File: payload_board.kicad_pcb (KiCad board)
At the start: 4 copper layers, 100 x 100 mm, 94 parts, among them IC1 RP2040_QFN56, IC2 AZ1117CH-3.3TRG1, J1 Cam_PicoLock, J12 5025700893, J12 FC Breakout, J15 SWC, J2 Cam_Conn, J2 Conn_ARM_JTAG_SWD_10, J3 Antenna_Conn, J4 usb jumper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

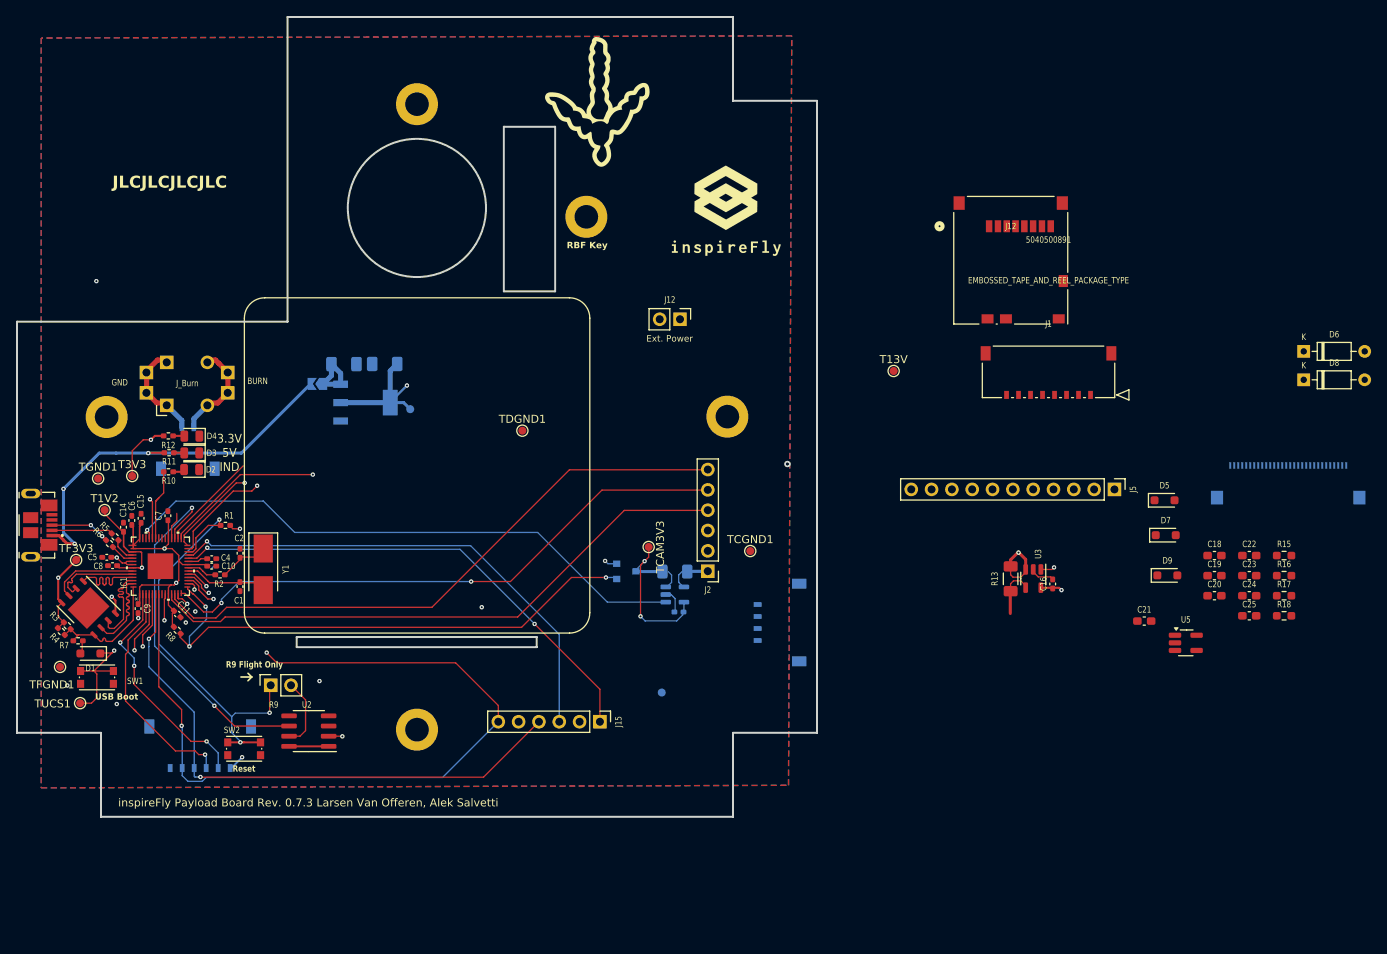
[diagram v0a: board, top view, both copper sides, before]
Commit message: Updated component placements and footprints
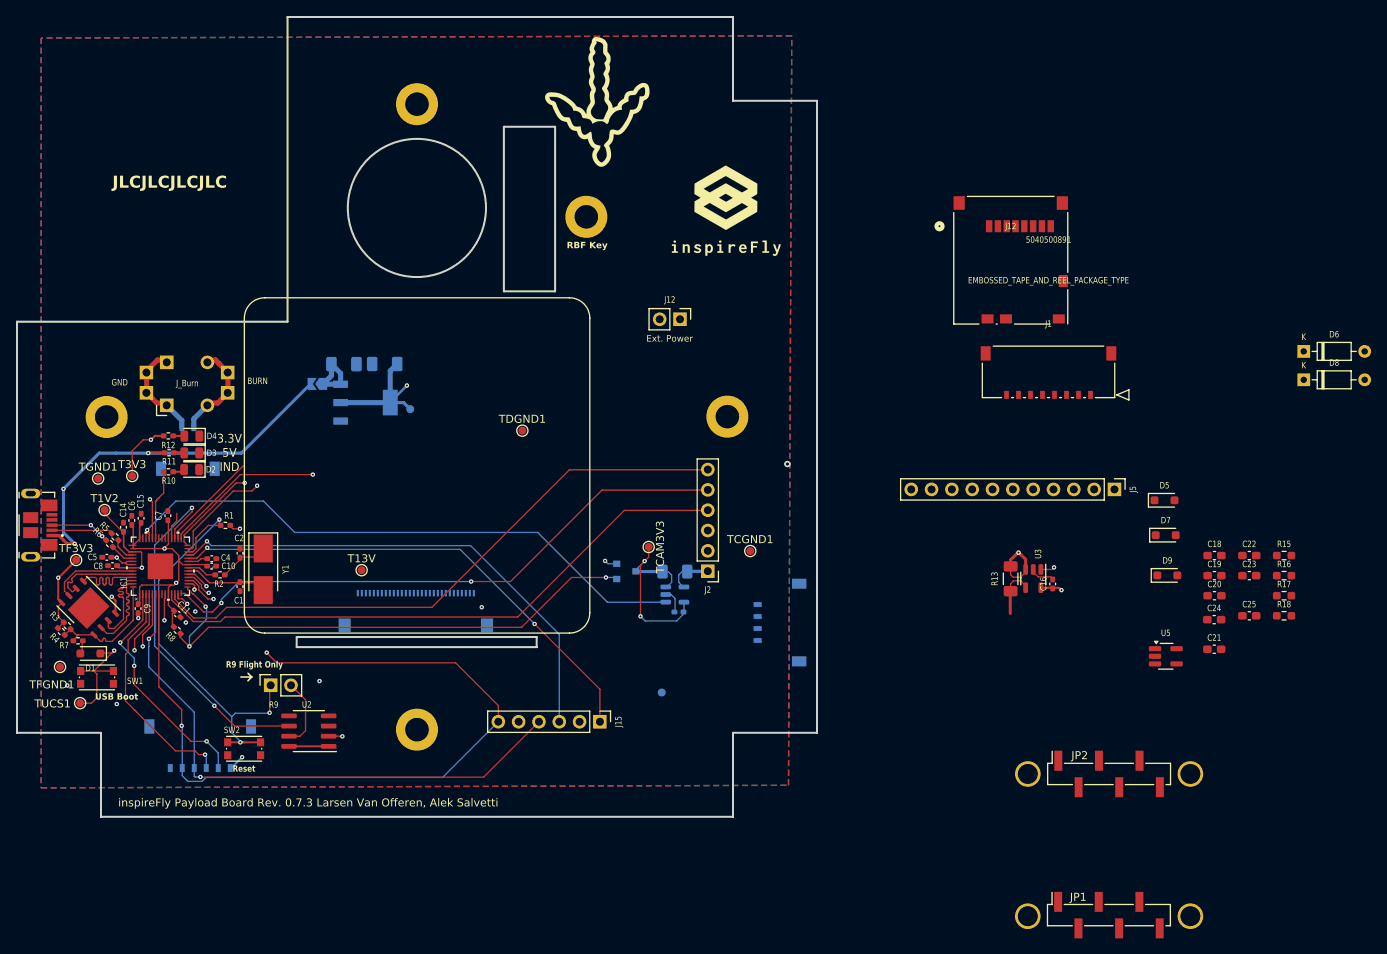
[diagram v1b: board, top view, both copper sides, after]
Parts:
- added ?: , , F.Cu at (159.7, 107.6)
- added ?: , , F.Cu at (139.3, 107.6)
- added ?: , , F.Cu at (159.7, 125.4)
- added ?: , , F.Cu at (139.3, 125.4)
- added JP1: , Connector_PinHeader_2.54mm:PinHeader_1x06_P2.54mm_Vertical_SMD_Pin1Right, F.Cu at (149.5, 125.3)
- added JP2: , Connector_PinHeader_2.54mm:PinHeader_1x06_P2.54mm_Vertical_SMD_Pin1Right, F.Cu at (149.5, 107.6)
- moved U6 110.2 mm to (62.8, 87.5)
- moved T13V 71.0 mm to (56.1, 82.2)
- moved C21 9.43 mm to (162.7, 92.0)
- moved C24 5.31 mm to (162.6, 88.3)
- moved U5 3.01 mm to (156.6, 92.9)
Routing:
- net GND: vias 9 -> 8
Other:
- board text added: "Keep Together. Mounting for IMU"

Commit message: Updated display footprints to reflect avaliability
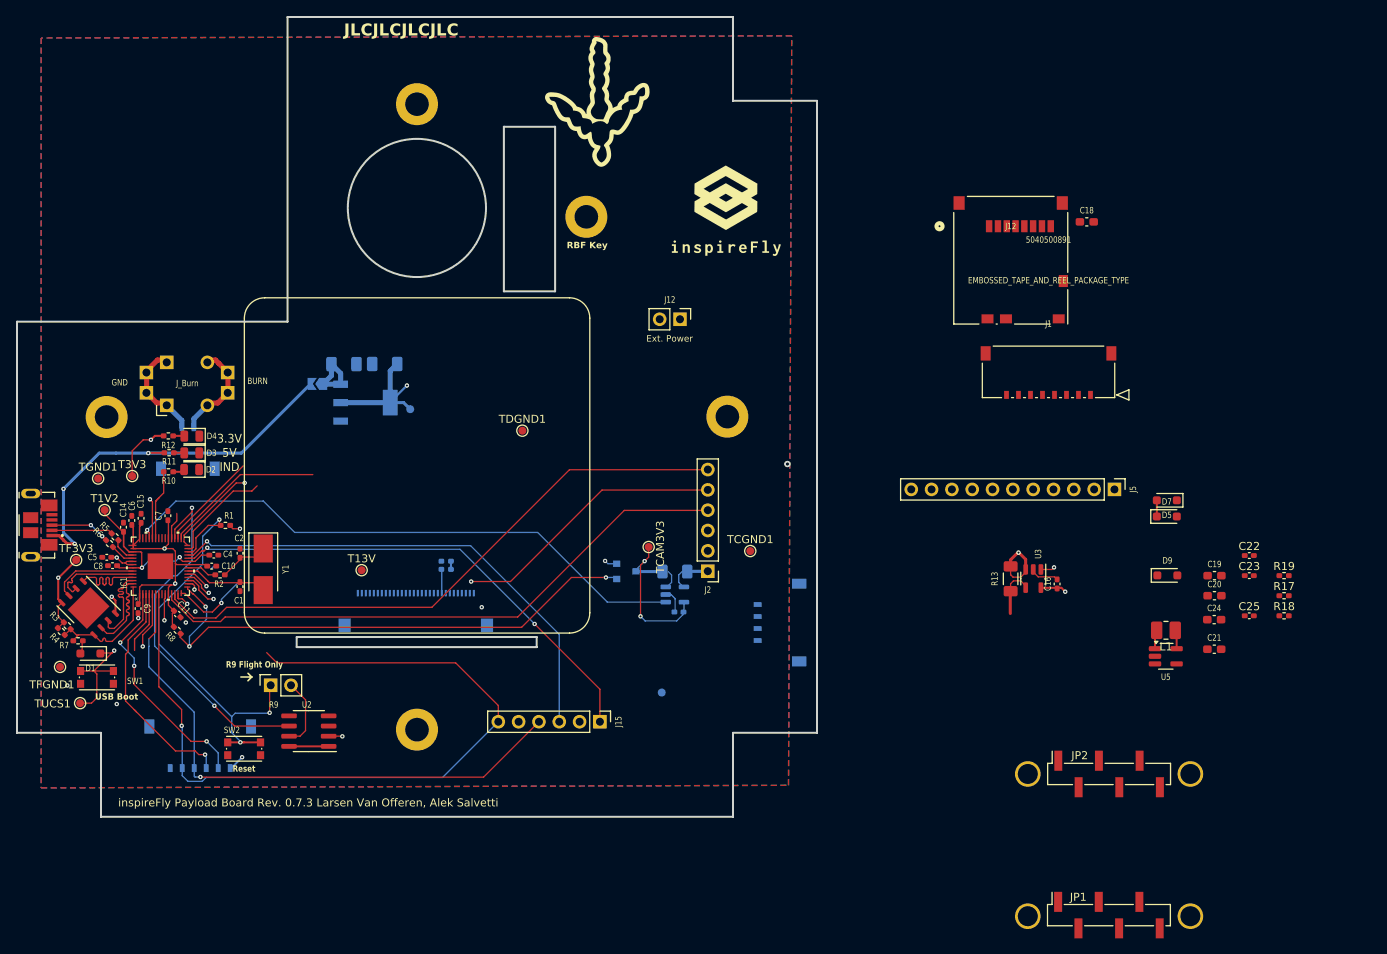
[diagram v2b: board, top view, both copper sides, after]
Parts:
- removed D6, D8: 1N4148, Diode_THT:D_DO-35_SOD27_P7.62mm_Horizontal
- added L1: 10uH/1A, Inductor_SMD:L_1008_2520Metric_Pad1.43x2.20mm_HandSolder, F.Cu at (156.6, 89.7)
- added R16: 300k, Resistor_SMD:R_0402_1005Metric_Pad0.72x0.64mm_HandSolder, B.Cu at (66.6, 81.0)
- C19: value 10u -> 10uF
- C22, C23, C25: footprint Capacitor_SMD:C_0603_1608Metric_Pad1.08x0.95mm_HandSolder -> Capacitor_SMD:C_0402_1005Metric_Pad0.74x0.62mm_HandSolder
- J2: value Conn_ARM_JTAG_SWD_10 -> (none)
- J5: value usb jumper -> (none)
- R15: value 600k -> 300k; footprint Resistor_SMD:R_0603_1608Metric_Pad0.98x0.95mm_HandSolder -> Resistor_SMD:R_0402_1005Metric_Pad0.72x0.64mm_HandSolder; moved to B.Cu
- R17, R18: footprint Resistor_SMD:R_0603_1608Metric_Pad0.98x0.95mm_HandSolder -> Resistor_SMD:R_0402_1005Metric_Pad0.72x0.64mm_HandSolder
- R19: renamed from R16; footprint Resistor_SMD:R_0603_1608Metric_Pad0.98x0.95mm_HandSolder -> Resistor_SMD:R_0402_1005Metric_Pad0.72x0.64mm_HandSolder
- moved R15 104.8 mm to (66.6, 82.0), turned to 180 degrees
- moved C18 44.7 mm to (146.7, 38.6)
- moved D7 2.34 mm to (156.7, 75.4)
- moved C16 0.55 mm to (143.0, 83.9)
- moved C4 0.52 mm to (37.6, 80.3)
- moved D5 0.29 mm to (156.7, 73.4), turned to 180 degrees
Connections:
- C19 pad 1: +3.3V -> DIN-
- C23 pad 2: +3.3V -> DIN-
- C24 pad 2: +3.3V -> DIN-
- R15 pad 1: GND -> Net-(R15-Pad1)
- U5 pad 4: +3.3V -> DIN-
- U5 pad 5: +3.3V -> DIN-
- U6 pad P$27: +3.3V -> DIN-
- U6 pad P$4: +3.3V -> DIN-
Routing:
- net SPI1_SCK_Cam: track 74.6 -> 2.08 mm
- net Disp_RST: track 62.9 -> 3.42 mm
- net I2C1_SDA: track 66.6 -> 7.88 mm, vias 2 -> 0
- net I2C1_SCL: track 63.2 -> 7.13 mm
- net UART1_TX: track 124.6 -> 71.6 mm, vias 2 -> 1
- net Disp_DC: track 54.3 -> 4.89 mm
- net ADC0: track 53.0 -> 6.86 mm
- net SD_IND: track 47.4 -> 3.74 mm
- net SPI0_SCK: track 52.6 -> 20.2 mm, vias 1 -> 0
- net SPI0_MISO: track 42.3 -> 13.1 mm, vias 1 -> 0
- net SPI1_MOSI_Cam: track 73.3 -> 44.3 mm
- net /USBBOOT: track 31.7 -> 17.0 mm
- net UART1_RX: track 114.7 -> 100.6 mm, vias 2 -> 1
- net Net-(U6-IREF): track 0.00 -> 3.00 mm
- net Net-(D9-A): track 0.00 -> 2.38 mm
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
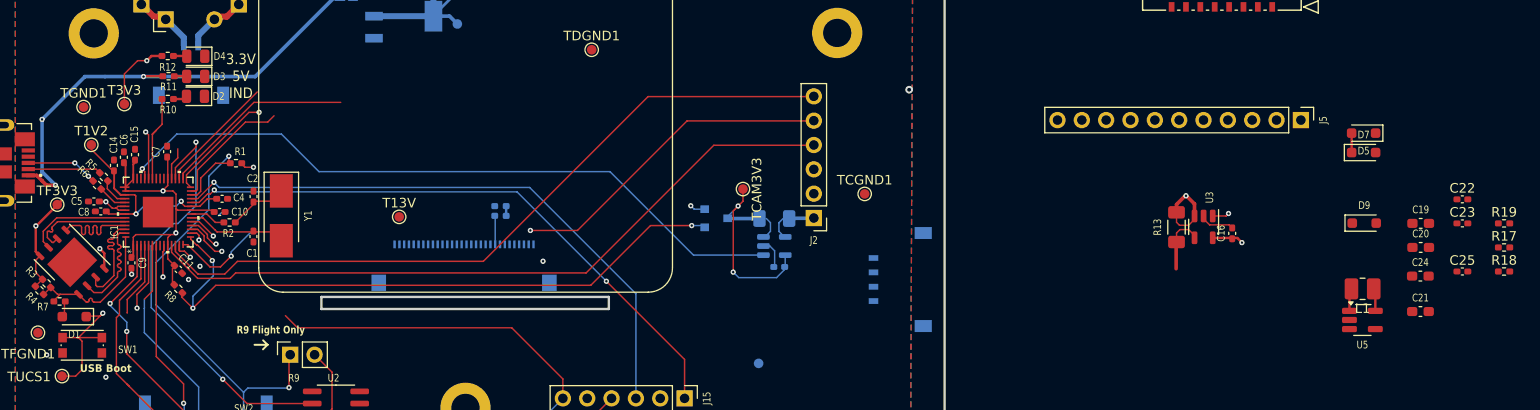
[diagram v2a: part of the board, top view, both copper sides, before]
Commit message: Changed the orientation of the connector to align, and moved a couple of the components Will continue tomorrow
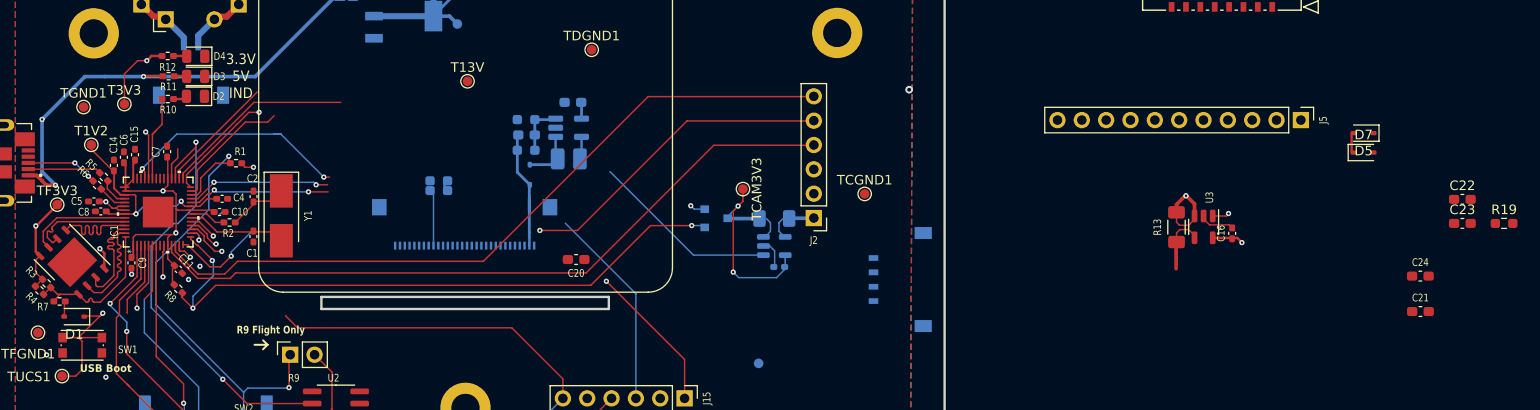
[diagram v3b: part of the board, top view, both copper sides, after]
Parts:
- C19, L1, U5: moved to B.Cu
- C22, C23: footprint Capacitor_SMD:C_0402_1005Metric_Pad0.74x0.62mm_HandSolder -> Capacitor_SMD:C_0603_1608Metric_Pad1.08x0.95mm_HandSolder
- C25: footprint Capacitor_SMD:C_0402_1005Metric_Pad0.74x0.62mm_HandSolder -> Capacitor_SMD:C_0603_1608Metric_Pad1.08x0.95mm_HandSolder; moved to B.Cu
- D1, D5, D7: footprint Diode_SMD:D_SOD-323_HandSoldering -> Diode_SMD:D_SOD-323
- D9: footprint Diode_SMD:D_SOD-323_HandSoldering -> Diode_SMD:D_SOD-323; moved to B.Cu
- R15, R16, R19: footprint Resistor_SMD:R_0402_1005Metric_Pad0.72x0.64mm_HandSolder -> Resistor_SMD:R_0603_1608Metric_Pad0.98x0.95mm_HandSolder
- R17, R18: footprint Resistor_SMD:R_0402_1005Metric_Pad0.72x0.64mm_HandSolder -> Resistor_SMD:R_0603_1608Metric_Pad0.98x0.95mm_HandSolder; moved to B.Cu
- moved R18 103.3 mm to (69.3, 72.0), turned to 180 degrees
- moved R17 102.6 mm to (69.3, 75.2)
- moved C25 98.7 mm to (69.4, 73.6)
- moved C19 89.4 mm to (74.2, 70.2), turned to 180 degrees
- moved C20 88.1 mm to (74.5, 86.6), turned to 180 degrees
- moved D9 87.2 mm to (69.7, 77.8), turned to 90 degrees
- moved U5 85.2 mm to (73.8, 72.8)
- moved L1 83.9 mm to (73.8, 76.1)
- moved T13V 15.8 mm to (63.2, 68.0)
- moved R15 6.96 mm to (60.2, 79.4)
- moved R16 6.96 mm to (60.2, 78.4)
- moved U6 4.77 mm to (62.9, 82.7), turned to 180 degrees
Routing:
- net SWCLK: track 63.4 -> 30.5 mm, vias 2 -> 3
- net ADC1: track 72.8 -> 44.5 mm, vias 1 -> 2
- net SWDIO: track 62.9 -> 36.4 mm, vias 1 -> 2
- net +13V: track 0.00 -> 13.3 mm
- net Net-(U5-FB): track 0.00 -> 5.42 mm
- net Net-(D9-A): track 2.38 -> 5.54 mm
- net Net-(U6-IREF): track 3.00 -> 5.77 mm
- net DIN-: track 8.48 -> 10.2 mm
- net SPI1_MOSI_Cam: track 44.3 -> 43.4 mm
- net Cam_RST: vias 4 -> 3

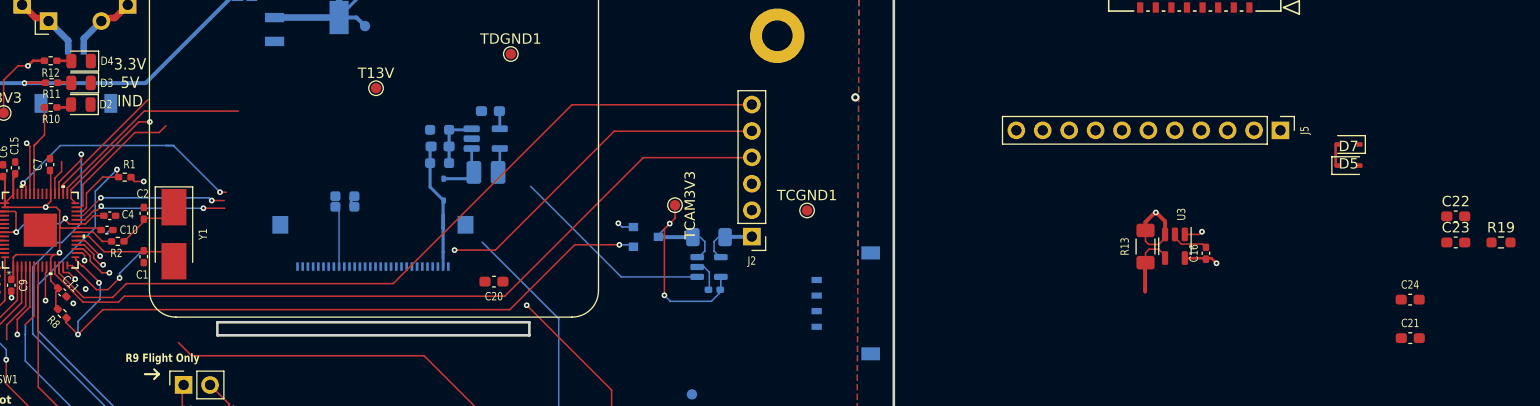
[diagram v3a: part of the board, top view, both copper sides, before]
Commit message: Rotated it back (by bad i dont know how to read schematics) and added some connections
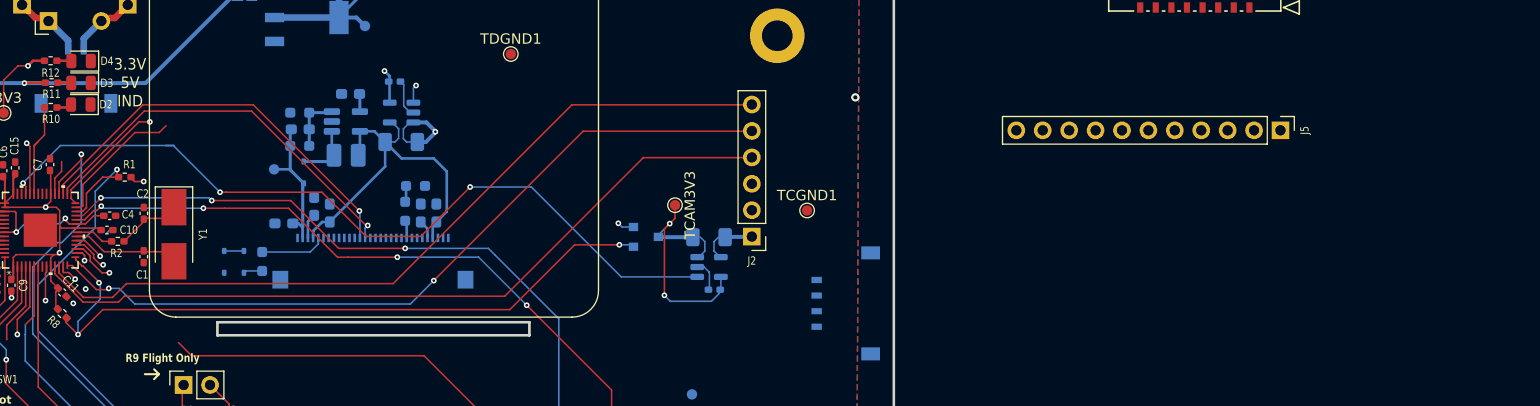
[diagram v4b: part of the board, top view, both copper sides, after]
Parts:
- C16, C20, C21, C22, C23, C24, D5, D7, R13, R19, T13V, U3: moved to B.Cu
- moved R19 119.1 mm to (52.2, 84.7), turned to 90 degrees
- moved D5 108.7 mm to (48.6, 84.7), turned to 90 degrees
- moved C23 108.3 mm to (58.8, 80.0), turned to -90 degrees
- moved D7 106.6 mm to (50.5, 84.7), turned to -90 degrees
- moved C21 106.2 mm to (57.2, 79.4), turned to -90 degrees
- moved C22 99.5 mm to (67.5, 80.0), turned to -90 degrees
- moved C24 94.0 mm to (69.0, 80.0), turned to -90 degrees
- moved C16 79.7 mm to (65.0, 67.4), turned to 0 degrees
- moved U3 75.5 mm to (65.7, 70.3), turned to 180 degrees
- moved R13 72.3 mm to (65.6, 73.2), turned to 0 degrees
- moved C20 21.0 mm to (54.3, 81.0), turned to 0 degrees
- moved C19 13.6 mm to (60.8, 68.5)
- moved D9 13.6 mm to (56.3, 76.1)
- moved L1 13.6 mm to (60.3, 74.4)
- moved R17 13.6 mm to (55.9, 73.5)
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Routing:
- net ADC1: track 44.5 -> 77.5 mm, vias 2 -> 3
- net SWCLK: track 30.5 -> 63.4 mm, vias 3 -> 4
- net SPI1_MOSI_Cam: track 43.4 -> 74.2 mm
- net SPI0_MOSI: track 12.5 -> 39.5 mm, vias 0 -> 1
- net DIN-: track 10.2 -> 36.9 mm
- net SWDIO: track 36.4 -> 63.0 mm, vias 2 -> 3
- net SPI0_SCK: track 20.2 -> 38.5 mm, vias 0 -> 1
- net Net-(U6-VSL): track 0.00 -> 6.29 mm
- net Net-(U6-IREF): track 5.77 -> 1.71 mm
- net Net-(U6-VCOMH): track 0.00 -> 2.42 mm
- net Net-(D7-A): track 0.00 -> 1.82 mm
- net Net-(U6-VDD): track 0.00 -> 1.81 mm
- net +13V: track 13.3 -> 14.9 mm
- net Net-(R15-Pad1): track 1.02 -> 1.56 mm

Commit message: Connected some more stuff
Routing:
- net SPI1_SCK_Cam: track 2.08 -> 73.6 mm, vias 1 -> 2
- net SPI0_CS_DISP: track 3.47 -> 43.7 mm, vias 0 -> 1
- net ADC0: track 6.86 -> 45.3 mm, vias 2 -> 3
- net Disp_RST: track 3.42 -> 41.7 mm, vias 1 -> 3
- net Disp_DC: track 4.89 -> 35.9 mm
- net SD_IND: track 3.74 -> 5.12 mm
- net Cam_RST: track 68.4 -> 69.4 mm
- net +3.3V: track 95.9 -> 95.4 mm
- net UART1_TX: vias 1 -> 2
- net GND: vias 8 -> 9
